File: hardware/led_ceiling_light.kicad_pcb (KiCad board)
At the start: 2 copper layers, 105 x 60 mm, 28 parts, among them J1 Screw_Terminal_01x03, Q1 BSS123, U1 AL8861

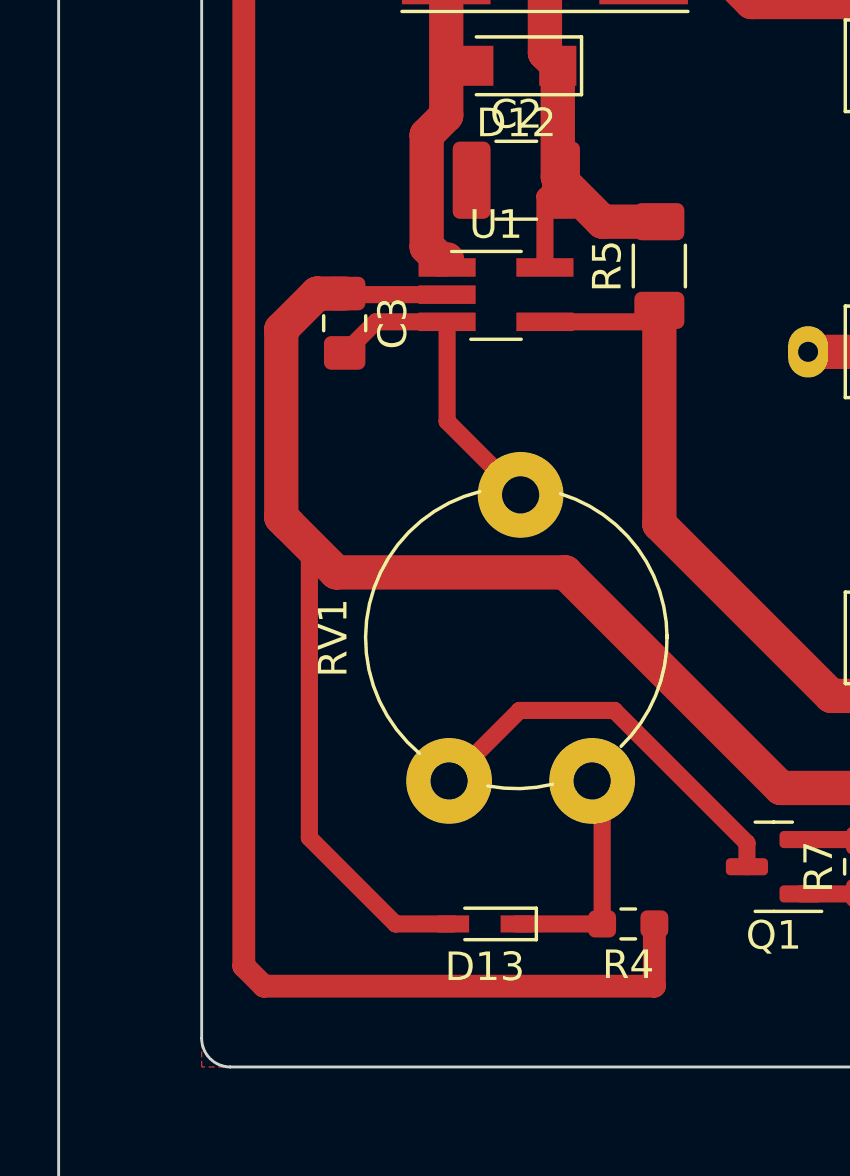
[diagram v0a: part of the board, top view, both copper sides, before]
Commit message: Fix D13 footprint
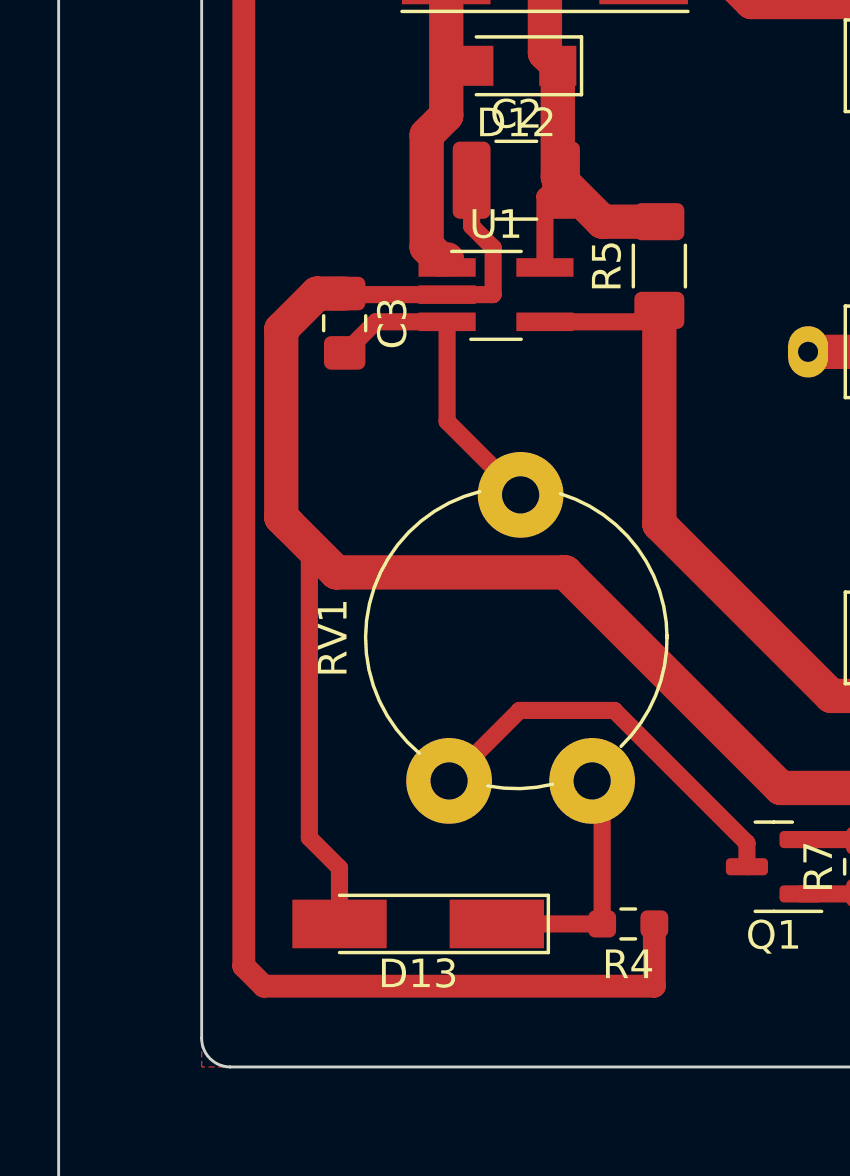
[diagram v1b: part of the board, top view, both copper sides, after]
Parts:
- D13: footprint Diode_SMD:D_SC-80_HandSoldering -> Diode_SMD:D_MiniMELF_Handsoldering
- moved D13 2.33 mm to (107.6, 105.0)
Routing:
- net GND: track 323.6 -> 326.7 mm
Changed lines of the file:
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@@
     )
   )
-  (footprint "Diode_SMD:D_SC-80_HandSoldering" (layer "F.Cu")
-    (at 109.9 105 180)
-    (descr "JEITA SC-80")
-    (tags "SC-80")
+  (footprint "Diode_SMD:D_MiniMELF_Handsoldering" (layer "F.Cu")
+    (at 107.569 105 180)
+    (descr "Diode Mini-MELF (SOD-80) Handsoldering")
+    (tags "Diode Mini-MELF (SOD-80) Handsoldering")
     (property "P/N" " ZMM5223B (M)")
     (property "Sheetfile" "led_ceiling_light.kicad_sch")
     (property "Sheetname" "")
     (attr smd)
-    (fp_text reference "D13" (at 0 -1.5) (layer "F.SilkS")
-      (effects (font (size 1 1) (thickness 0.15)))
-    )
-    (fp_text value "2.7V" (at 0 1.6) (layer "F.Fab")
-      (effects (font (size 1 1) (thickness 0.15)))
-    )
-    (fp_text user "${REFERENCE}" (at 0 -1.5) (layer "F.Fab")
-      (effects (font (size 1 1) (thickness 0.15)))
-    )
-    (fp_line (start -1.8 0.55) (end 0.7 0.55) (layer "F.SilkS") (width 0.12))
-    (fp_line (start -1.8 -0.55) (end -1.8 0.55) (layer "F.SilkS") (width 0.12))
-    (fp_line (start -1.8 -0.55) (end 0.7 -0.55) (layer "F.SilkS") (width 0.12))
-    (fp_line (start -1.9 0.7) (end 1.9 0.7) (layer "F.CrtYd") (width 0.05))
-    (fp_line (start 1.9 -0.7) (end 1.9 0.7) (layer "F.CrtYd") (width 0.05))
-    (fp_line (start 1.9 -0.7) (end -1.9 -0.7) (layer "F.CrtYd") (width 0.05))
-    (fp_line (start -1.9 0.7) (end -1.9 -0.7) (layer "F.CrtYd") (width 0.05))
-    (fp_line (start 0.2 -0.225) (end 0.2 0.225) (layer "F.Fab") (width 0.1))
-    (fp_line (start 0.2 0.225) (end -0.2 0) (layer "F.Fab") (width 0.1))
-    (fp_line (start -0.65 -0.4) (end 0.65 -0.4) (layer "F.Fab") (width 0.1))
-    (fp_line (start 0.65 0.4) (end -0.65 0.4) (layer "F.Fab") (width 0.1))
-    (fp_line (start -0.65 0.4) (end -0.65 -0.4) (layer "F.Fab") (width 0.1))
-    (fp_line (start 0.2 0) (end 0.45 0) (layer "F.Fab") (width 0.1))
-    (fp_line (start -0.2 -0.275) (end -0.2 0.275) (layer "F.Fab") (width 0.1))
-    (fp_line (start -0.2 0) (end -0.475 0) (layer "F.Fab") (width 0.1))
-    (fp_line (start -0.2 0) (end 0.2 -0.225) (layer "F.Fab") (width 0.1))
-    (fp_line (start 0.65 -0.4) (end 0.65 0.4) (layer "F.Fab") (width 0.1))
-    (pad "1" smd rect (at -1.1 0 180) (size 1.1 0.6) (layers "F.Cu" "F.Paste" "F.Mask")
+    (fp_text reference "D13" (at 0 -1.75 180) (layer "F.SilkS")
+      (effects (font (size 1 1) (thickness 0.15)))
+    )
+    (fp_text value "2.7V" (at 0 1.75 180) (layer "F.Fab")
+      (effects (font (size 1 1) (thickness 0.15)))
+    )
+    (fp_text user "${REFERENCE}" (at 0 -1.75 180) (layer "F.Fab")
+      (effects (font (size 1 1) (thickness 0.15)))
+    )
+    (fp_line (start -4.55 -1) (end -4.55 1) (layer "F.SilkS") (width 0.12))
+    (fp_line (start -4.55 1) (end 2.75 1) (layer "F.SilkS") (width 0.12))
+    (fp_line (start 2.75 -1) (end -4.55 -1) (layer "F.SilkS") (width 0.12))
+    (fp_line (start 4.65 1.1) (end -4.65 1.1) (layer "F.CrtYd") (width 0.05))
+    (fp_line (start -4.65 -1.1) (end 4.65 -1.1) (layer "F.CrtYd") (width 0.05))
+    (fp_line (start 4.65 -1.1) (end 4.65 1.1) (layer "F.CrtYd") (width 0.05))
+    (fp_line (start -4.65 1.1) (end -4.65 -1.1) (layer "F.CrtYd") (width 0.05))
+    (fp_line (start -1.65 0.8) (end -1.65 -0.8) (layer "F.Fab") (width 0.1))
+    (fp_line (start 1.65 0.8) (end -1.65 0.8) (layer "F.Fab") (width 0.1))
+    (fp_line (start -0.35 0) (end 0.25 -0.4) (layer "F.Fab") (width 0.1))
+    (fp_line (start -0.35 0) (end -0.35 0.55) (layer "F.Fab") (width 0.1))
+    (fp_line (start -1.65 -0.8) (end 1.65 -0.8) (layer "F.Fab") (width 0.1))
+    (fp_line (start 0.25 0) (end 0.75 0) (layer "F.Fab") (width 0.1))
+    (fp_line (start 1.65 -0.8) (end 1.65 0.8) (layer "F.Fab") (width 0.1))
+    (fp_line (start -0.35 0) (end -0.35 -0.55) (layer "F.Fab") (width 0.1))
+    (fp_line (start -0.75 0) (end -0.35 0) (layer "F.Fab") (width 0.1))
+    (fp_line (start 0.25 -0.4) (end 0.25 0.4) (layer "F.Fab") (width 0.1))
+    (fp_line (start 0.25 0.4) (end -0.35 0) (layer "F.Fab") (width 0.1))
+    (pad "1" smd rect (at -2.75 0 180) (size 3.3 1.7) (layers "F.Cu" "F.Paste" "F.Mask")
       (net 17 "Net-(D13-Pad1)") (pinfunction "K") (pintype "passive"))
-    (pad "2" smd rect (at 1.1 0 180) (size 1.1 0.6) (layers "F.Cu" "F.Paste" "F.Mask")
+    (pad "2" smd rect (at 2.75 0 180) (size 3.3 1.7) (layers "F.Cu" "F.Paste" "F.Mask")
       (net 1 "GND") (pinfunction "A") (pintype "passive"))
-    (model "${KICAD6_3DMODEL_DIR}/Diode_SMD.3dshapes/D_SC-80.wrl"
+    (model "${KICAD6_3DMODEL_DIR}/Diode_SMD.3dshapes/D_MiniMELF.wrl"
       (offset (xyz 0 0 0))
       (scale (xyz 1 1 1))
@@
   (gr_rect locked (start 100 110) (end 106 104) (layer "User.1") (width 0.15) (fill solid))
   (gr_rect locked (start 195 110) (end 189 104) (layer "User.1") (width 0.15) (fill solid))
+  (segment (start 104.819 105) (end 104.819 103.041) (width 0.6) (layer "F.Cu") (net 1))
   (segment (start 120.9375 102.05) (end 122.9625 102.05) (width 0.6) (layer "F.Cu") (net 1))
+  (segment (start 110.19 82.99) (end 110.19 81.361) (width 0.6) (layer "F.Cu") (net 1))
+  (segment (start 109.4375 80.6085) (end 109.4375 79) (width 0.6) (layer "F.Cu") (net 1))
   (segment (start 123.246361 100.246361) (end 120.246361 100.246361) (width 1.2) (layer "F.Cu") (net 1))
   (segment (start 181.991 81.7) (end 181.991 71.991) (width 0.6) (layer "F.Cu") (net 1))
@@
   (segment (start 184.023 95.631) (end 179.407639 100.246361) (width 1.2) (layer "F.Cu") (net 1))
   (segment (start 177 67) (end 122.626 67) (width 0.6) (layer "F.Cu") (net 1))
+  (segment (start 110.18 83) (end 110.19 82.99) (width 0.6) (layer "F.Cu") (net 1))
+  (segment (start 110.19 81.361) (end 109.4375 80.6085) (width 0.6) (layer "F.Cu") (net 1))
   (segment (start 108.58 83) (end 105.0375 83) (width 0.6) (layer "F.Cu") (net 1))
   (segment (start 102.783 84.217) (end 104.0375 82.9625) (width 1.2) (layer "F.Cu") (net 1))
-  (segment (start 106.778 105) (end 103.765 101.987) (width 0.6) (layer "F.Cu") (net 1))
   (segment (start 187.3885 62) (end 192.913 67.5245) (width 0.6) (layer "F.Cu") (net 1))
   (segment (start 122 64) (end 122 62.912) (width 0.6) (layer "F.Cu") (net 1))
+  (segment (start 104.819 103.041) (end 103.765 101.987) (width 0.6) (layer "F.Cu") (net 1))
   (segment (start 184.023 84.963) (end 187.198 84.963) (width 1.2) (layer "F.Cu") (net 1))
   (segment (start 122 65.3) (end 122 64) (width 0.4) (layer "F.Cu") (net 1))
@@
   (segment (start 182.118 77.216) (end 182.118 83.058) (width 1.2) (layer "F.Cu") (net 1))
   (segment (start 123 102.0875) (end 123 100.492722) (width 0.6) (layer "F.Cu") (net 1))
-  (segment (start 108.8 105) (end 106.778 105) (width 0.6) (layer "F.Cu") (net 1))
   (segment (start 122 62.912) (end 122.912 62) (width 0.6) (layer "F.Cu") (net 1))
   (segment (start 187 94.455) (end 184.498 94.455) (width 1.2) (layer "F.Cu") (net 1))
@@
   (segment (start 192.913 82.913) (end 190.863 84.963) (width 0.6) (layer "F.Cu") (net 1))
   (segment (start 187 75.598) (end 183.736 75.598) (width 1.2) (layer "F.Cu") (net 1))
+  (segment (start 103.765 91.765) (end 103 91) (width 0.6) (layer "F.Cu") (net 1))
   (segment (start 120.246361 100.246361) (end 112.71 92.71) (width 1.2) (layer "F.Cu") (net 1))
   (segment (start 104.0375 82.9625) (end 105 82.9625) (width 1.2) (layer "F.Cu") (net 1))
   (segment (start 123 100.492722) (end 123.246361 100.246361) (width 0.6) (layer "F.Cu") (net 1))
-  (segment (start 103.765 91.765) (end 103 91) (width 0.6) (layer "F.Cu") (net 1))
+  (segment (start 103.765 101.987) (end 103.765 91.765) (width 0.6) (layer "F.Cu") (net 1))
   (segment (start 122.626 67) (end 122 66.374) (width 0.6) (layer "F.Cu") (net 1))
   (segment (start 192.913 67.5245) (end 192.913 82.913) (width 0.6) (layer "F.Cu") (net 1))
@@
   (segment (start 184.023 84.963) (end 184.023 93.98) (width 1.2) (layer "F.Cu") (net 1))
   (segment (start 184.023 93.98) (end 184.023 95.631) (width 1.2) (layer "F.Cu") (net 1))
-  (segment (start 103.765 101.987) (end 103.765 91.765) (width 0.6) (layer "F.Cu") (net 1))
   (segment (start 183.736 75.598) (end 182.118 77.216) (width 1.2) (layer "F.Cu") (net 1))
   (segment (start 181.991 71.991) (end 177 67) (width 0.6) (layer "F.Cu") (net 1))
+  (segment (start 108.58 83) (end 110.18 83) (width 0.6) (layer "F.Cu") (net 1))
   (segment (start 104.71 92.71) (end 103 91) (width 1.2) (layer "F.Cu") (net 1))
   (segment (start 112.71 92.71) (end 104.71 92.71) (width 1.2) (layer "F.Cu") (net 1))
